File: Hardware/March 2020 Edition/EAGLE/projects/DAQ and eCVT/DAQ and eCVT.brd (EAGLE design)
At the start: 88.9 x 114 mm, 21 parts, among them J1 5558342-1, J2 5558342-1, J3 5558342-1, J4 5558342-1, U1 AP2114H-3.3TRG1

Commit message: Wiring the board...
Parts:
- removed D1: LTST-C170TBKT, LED:DIOC200X125X110
- added LED1: (no value), led:CHIPLED_0805
- moved R5 16.5 mm to (-3.81, 73.7)
- moved C1 7.41 mm to (31.8, 50.8)
- moved C2 7.41 mm to (31.8, 55.9)
- moved U1 7.41 mm to (25.4, 53.3)
- moved R1 2.54 mm to (8.89, 78.7)
- moved R3 2.54 mm to (8.89, 82.5)
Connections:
- removed net DAQ_ECVT\_MISO: U$31.12/MISO
- removed net N$34: D1.-, R5.1
- new net N$1: LED1.A, R5.2
- net +3V3: now also R5.1; no longer D1.+
- net DAQ_ECVT_MISO: now also U$31.12/MISO
- net GND: now also LED1.C; no longer R5.2
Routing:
- net DAQ_XBEE_MISO: track 0.00 -> 84.9 mm
- net DAQ_XBEE_RX: track 9.86 -> 68.3 mm, vias 0 -> 1
- net DAQ_XBEE_TX: track 9.09 -> 67.3 mm
- net DAQ_ECVT_TX: track 0.00 -> 19.9 mm, vias 0 -> 1
- net DAQ_ECVT_MOSI: track 0.00 -> 18.8 mm
- net DAQ_ECVT_MISO: track 0.00 -> 18.8 mm
- net DAQ_ECVT_SCK: track 0.00 -> 18.8 mm
- net DAQ_ECVT_CS: track 0.00 -> 13.2 mm
- net RBRAKE_PRESSURE: track 38.2 -> 35.7 mm
- net FBRAKE_PRESSURE: track 36.9 -> 34.4 mm
- net FRWHEEL_SPEED: track 84.2 -> 86.3 mm
- net SMOT_INB: track 54.1 -> 55.9 mm
- net SENC_A: track 59.1 -> 60.8 mm
- net DAQ_XBEE_MOSI: track 72.6 -> 73.9 mm
- net SMOT_INA: track 48.6 -> 49.8 mm
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
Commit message: Wiring the board...
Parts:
- moved C1 6.84 mm to (25.4, 48.3)
- moved C2 6.84 mm to (25.4, 58.4)
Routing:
- net DAQ_SPARE_A17_PWM: track 0.00 -> 52.8 mm, vias 0 -> 1
- net DAQ_SPARE_A18_PWM_SCL: track 0.00 -> 48.9 mm, vias 0 -> 1
- net DAQ_SPARE_A16_PWM: track 0.00 -> 48.0 mm, vias 0 -> 1
- net SMOT_CS: track 0.00 -> 47.4 mm, vias 0 -> 1
- net DAQ_SPARE_A21_DAC0: track 0.00 -> 47.2 mm, vias 0 -> 1
- net DAQ_SPARE_A19_PWM_SDA: track 0.00 -> 46.4 mm, vias 0 -> 1
- net DAQ_SPARE_A22_DAC1: track 0.00 -> 45.4 mm, vias 0 -> 1
- net PMOT_CS: track 0.00 -> 41.0 mm, vias 0 -> 3
- net ECVT_SPARE_A22_DAC1: track 0.00 -> 26.5 mm
- net ECVT_SPARE_A21_DAC0: track 0.00 -> 22.3 mm
- net DAQ_ECVT_CS: track 13.2 -> 18.8 mm, vias 0 -> 1
- net FLWHEEL_SPEED: track 81.2 -> 76.0 mm
- net FRWHEEL_SPEED: track 86.3 -> 81.1 mm
- net RBRAKE_PRESSURE: track 35.7 -> 38.2 mm
- net PMOT_INB: track 36.0 -> 37.8 mm
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
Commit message: Wiring the board...
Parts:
- moved C1 38.2 mm to (-12.7, 45.7)
- moved C2 38.2 mm to (-12.7, 55.9)
- moved U1 38.2 mm to (-12.7, 50.8)
- moved R5 9.25 mm to (-12.7, 76.2)
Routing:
- net DAQ_SPARE_A16_PWM: track 48.0 -> 120.1 mm
- net DAQ_SPARE_A17_PWM: track 52.8 -> 124.7 mm, vias 1 -> 3
- net DAQ_SPARE_A18_PWM_SCL: track 48.9 -> 118.2 mm
- net DAQ_SPARE_A19_PWM_SDA: track 46.4 -> 113.2 mm
- net DAQ_SPARE_A21_DAC0: track 47.2 -> 113.7 mm, vias 1 -> 3
- net DAQ_SPARE_A22_DAC1: track 45.4 -> 109.4 mm
- net ECVT_SPARE_A22_DAC1: track 26.5 -> 90.4 mm, vias 0 -> 4
- net ECVT_SPARE_A21_DAC0: track 22.3 -> 84.5 mm
- net PMOT_CS: track 41.0 -> 33.7 mm, vias 3 -> 2
- net FRWHEEL_SPEED: track 81.1 -> 83.1 mm
- net FLWHEEL_SPEED: track 76.0 -> 78.0 mm
- net RBRAKE_PRESSURE: track 38.2 -> 36.7 mm
- net FBRAKE_PRESSURE: track 34.4 -> 34.9 mm
- net RWHEELS_SPEED: vias 1 -> 2
- net ENGINE_SPEED: vias 2 -> 1

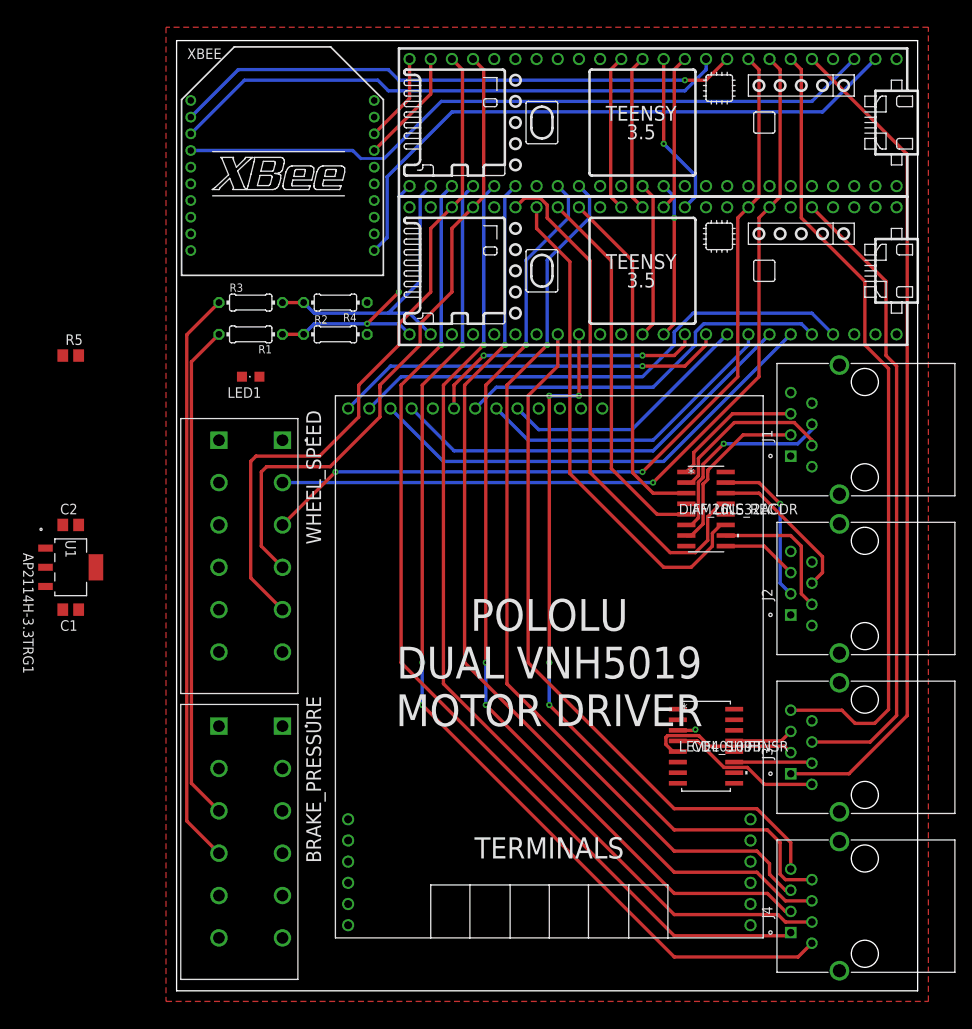
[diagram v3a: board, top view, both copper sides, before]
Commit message: Checkpoint before rewiring spring terminals to front/back instead of wheelspeed/brakepressure
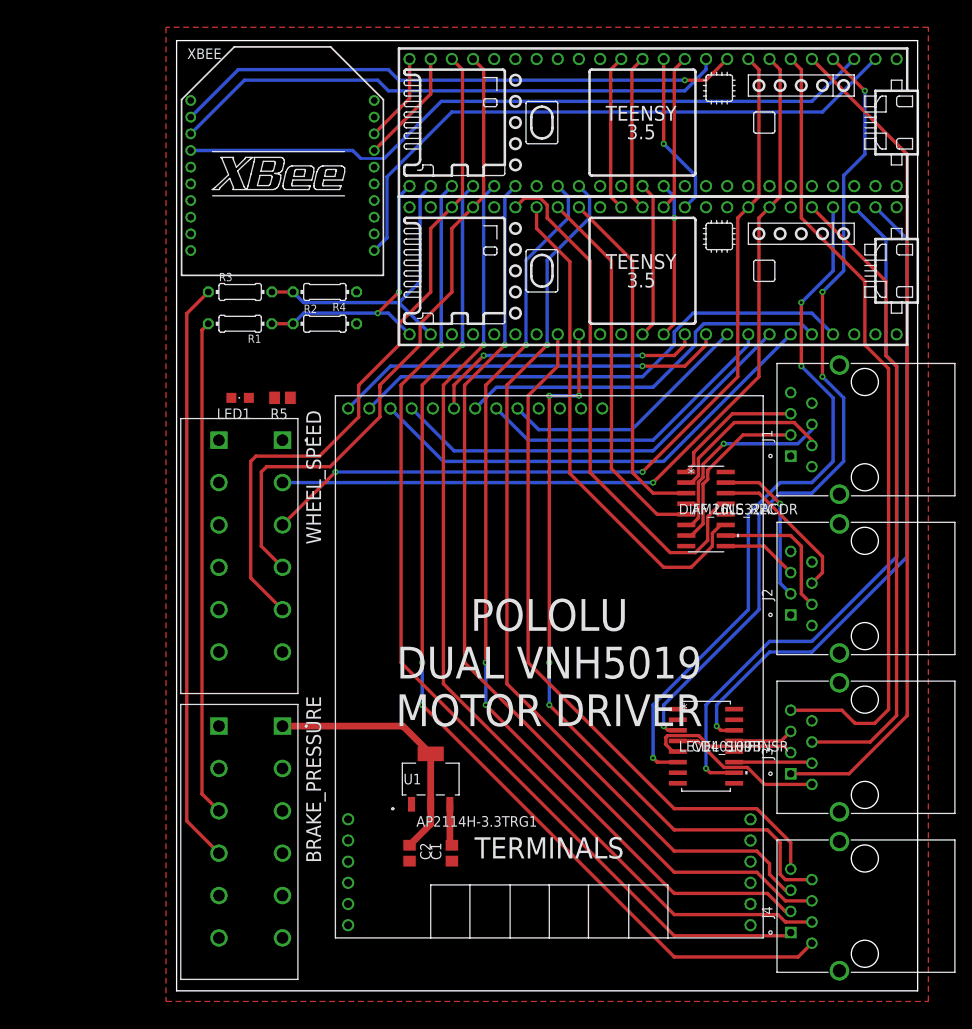
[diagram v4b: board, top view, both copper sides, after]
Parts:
- moved C2 56.6 mm to (27.9, 16.5), turned to 270 degrees
- moved C1 54.3 mm to (33.0, 16.5), turned to 270 degrees
- moved U1 50.1 mm to (30.5, 25.4), turned to 0 degrees
- moved R5 25.9 mm to (12.7, 71.1), turned to 180 degrees
- moved LED1 2.84 mm to (7.62, 71.1)
- moved R1 1.80 mm to (7.62, 80.0)
- moved R2 1.80 mm to (17.8, 80.0)
- moved R3 1.80 mm to (7.62, 83.8)
- moved R4 1.80 mm to (17.8, 83.8)
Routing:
- net DAQ_STATUS_LED: track 2.15 -> 97.8 mm, vias 1 -> 4
- net BKSHIFT_LED: track 0.00 -> 85.4 mm, vias 0 -> 1
- net ECVT_STATUS_LED: track 0.00 -> 83.6 mm, vias 0 -> 3
- net UPSHIFT_LED: track 0.00 -> 78.6 mm, vias 0 -> 1
- net +3V3: track 0.00 -> 31.2 mm
- net +5V: track 0.00 -> 5.01 mm
- net RBRAKE_PRESSURE_W/O_RES: track 69.2 -> 70.0 mm

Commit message: Almost done wiring the board!
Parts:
- moved R1 1.27 mm to (7.62, 81.3), turned to 0 degrees
- moved R2 1.27 mm to (17.8, 81.3)
- turned R4 to 0 degrees
- renumbered BRAKE_PRESSURE to FRONT_SENSORS, WHEEL_SPEED to REAR_SENSORS
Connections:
- net N$1 renamed LED
- removed net FBRAKE_PRESSURE_W/O_RES: FRONT_SENSORS.3_A, FRONT_SENSORS.3_B, R1.2
- removed net RBRAKE_PRESSURE_W/O_RES: FRONT_SENSORS.4_A, FRONT_SENSORS.4_B, R3.1
- new net FBRAKE_PRESSURE_BEFORE_RESISTORS: FRONT_SENSORS.5_A, FRONT_SENSORS.5_B, R3.1
- new net RBRAKE_PRESSURE_BEFORE_RESISTORS: R1.1, REAR_SENSORS.5_A, REAR_SENSORS.5_B
- net +3V3: now also REAR_SENSORS.1_A, REAR_SENSORS.1_B
- net +5V: now also REAR_SENSORS.2_A, REAR_SENSORS.2_B; no longer REAR_SENSORS.1_A, REAR_SENSORS.1_B
- net ENGINE_SPEED: now also REAR_SENSORS.3_A, REAR_SENSORS.3_B; no longer REAR_SENSORS.2_A, REAR_SENSORS.2_B
- net FBRAKE_PRESSURE: now also R3.2, R4.2; no longer R1.1, R2.1
- net FLWHEEL_SPEED: now also FRONT_SENSORS.3_A, FRONT_SENSORS.3_B; no longer REAR_SENSORS.4_A, REAR_SENSORS.4_B
- net FRWHEEL_SPEED: now also FRONT_SENSORS.4_A, FRONT_SENSORS.4_B; no longer REAR_SENSORS.5_A, REAR_SENSORS.5_B
- net GND: now also R2.1; no longer FRONT_SENSORS.5_A, FRONT_SENSORS.5_B, R2.2
- net RBRAKE_PRESSURE: now also R1.2, R2.2; no longer R3.2, R4.2
- net RWHEELS_SPEED: now also REAR_SENSORS.4_A, REAR_SENSORS.4_B; no longer REAR_SENSORS.3_A, REAR_SENSORS.3_B
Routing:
- net +5V: track 5.01 -> 164.5 mm, vias 0 -> 4
- net FBRAKE_PRESSURE_BEFORE_RESISTORS: track 0.00 -> 75.1 mm
- net RBRAKE_PRESSURE_W/O_RES: track 70.0 -> 0.00 mm
- net FBRAKE_PRESSURE_W/O_RES: track 59.6 -> 0.00 mm
- net +12V: track 0.00 -> 44.9 mm, vias 0 -> 2
- net RBRAKE_PRESSURE_BEFORE_RESISTORS: track 0.00 -> 37.1 mm
- net FRWHEEL_SPEED: track 83.1 -> 113.4 mm
- net FLWHEEL_SPEED: track 78.0 -> 108.3 mm
- net GND: track 0.00 -> 25.4 mm, vias 0 -> 5
- net RWHEELS_SPEED: track 101.7 -> 110.3 mm, vias 2 -> 1
- net RBRAKE_PRESSURE: track 36.7 -> 40.1 mm
- net +3V3: track 31.2 -> 34.5 mm, vias 0 -> 4
- net LED: track 0.00 -> 3.08 mm
- net FBRAKE_PRESSURE: track 34.9 -> 37.5 mm, vias 2 -> 1
- net ENGINE_SPEED: track 102.1 -> 104.2 mm
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- added copper zone on layer 16, net +3V3

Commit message: No DRC errors! Need to do a final check + board writing
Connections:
- removed net N$19: U$33.3V3
- removed net N$2: U$31.3V3
- net +3V3: now also U$31.3V3, U$33.3V3
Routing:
- net +5V: track 164.5 -> 179.7 mm
- net RWHEELS_SPEED: track 110.3 -> 118.7 mm, vias 1 -> 2
- net FRWHEEL_SPEED: track 113.4 -> 121.0 mm
- net FLWHEEL_SPEED: track 108.3 -> 115.9 mm
- net FBRAKE_PRESSURE_BEFORE_RESISTORS: track 75.1 -> 82.7 mm
- net ENGINE_SPEED: track 104.2 -> 111.8 mm
- net RBRAKE_PRESSURE_BEFORE_RESISTORS: track 37.1 -> 44.8 mm
- net +3V3: track 34.5 -> 38.3 mm, vias 4 -> 6
- net DAQ_STATUS_LED_12V: track 18.8 -> 18.2 mm

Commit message: Small board revisions before sending out
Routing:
- net +5V: track 179.7 -> 207.9 mm, vias 4 -> 5
- net DAQ_SPARE_A17_PWM: track 125.6 -> 126.5 mm, vias 4 -> 3
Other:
- board text added: "+3.3V OUT +5V IN/OUT ENGINE IN RWHEELS IN RBRAKES IN GROUND"
- board text added: "+3.3V OUT +5V IN/OUT FLWHEEL IN FRWHEEL IN FBRAKES IN GROUND"
- board text added: "DASHBOARD"
- board text added: "DESIGNED BY RAHUL GOYAL MARCH 2020"
- board text added: "PRIMARY ENCODER"
- board text added: "SECONDARY ENCODER"
- board text added: "SPARES"
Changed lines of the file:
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@@
 <drawing>
 <settings>
-<setting alwaysvectorfont="no"/>
+<setting alwaysvectorfont="yes"/>
 <setting verticaltext="up"/>
 </settings>
@@
 <wire x1="88.88" y1="113.97" x2="0" y2="113.97" width="0" layer="20"/>
 <wire x1="0" y1="113.97" x2="0" y2="0" width="0" layer="20"/>
-<hole x="19.05" y="76.2" drill="4.3053"/>
-<hole x="19.05" y="3.175" drill="4.3053"/>
-<hole x="69.85" y="3.175" drill="4.3053"/>
+<hole x="19.05" y="76.2" drill="3.6576"/>
+<hole x="22.225" y="3.175" drill="3.6576"/>
+<hole x="66.675" y="3.175" drill="3.6576"/>
+<text x="9.525" y="76.2" size="1.27" layer="25" font="vector" ratio="25" align="center">DESIGNED BY
+RAHUL GOYAL
+MARCH 2020</text>
+<text x="44.45" y="86.36" size="2.54" layer="26" font="vector" ratio="25" rot="MR0" align="center">DESIGNED BY
+RAHUL GOYAL
+MARCH 2020</text>
+<text x="25.4" y="40.005" size="1.6764" layer="26" font="vector" ratio="25" rot="MR0" align="bottom-right">+3.3V OUT
++5V IN/OUT
+ENGINE IN
+RWHEELS IN
+RBRAKES IN
+GROUND</text>
+<text x="25.4" y="5.715" size="1.6764" layer="26" font="vector" ratio="25" rot="MR0" align="bottom-right">+3.3V OUT
++5V IN/OUT
+FLWHEEL IN
+FRWHEEL IN
+FBRAKES IN
+GROUND</text>
+<text x="63.5" y="10.16" size="1.6764" layer="26" font="vector" ratio="25" rot="MR0" align="center-left">SPARES</text>
+<text x="63.5" y="29.21" size="1.6764" layer="26" font="vector" ratio="25" rot="MR0" align="center-left">DASHBOARD</text>
+<text x="63.5" y="48.26" size="1.6764" layer="26" font="vector" ratio="25" rot="MR0" align="center-left">SECONDARY
+ENCODER</text>
+<text x="63.5" y="67.31" size="1.6764" layer="26" font="vector" ratio="25" rot="MR0" align="center-left">PRIMARY
+ENCODER</text>
 </plain>
 <attributes>
@@
 <contactref element="REAR_SENSORS" pad="3_A"/>
 <contactref element="REAR_SENSORS" pad="3_B"/>
-<wire x1="58.42" y1="62.23" x2="52.07" y2="55.88" width="0.4064" layer="16"/>
-<wire x1="52.07" y1="55.88" x2="12.7" y2="55.88" width="0.4064" layer="16"/>
 <wire x1="5.08" y1="55.88" x2="12.7" y2="55.88" width="0.4064" layer="16"/>
+<wire x1="12.7" y1="55.88" x2="13.97" y2="57.15" width="0.4064" layer="16"/>
+<wire x1="53.34" y1="57.15" x2="58.42" y2="62.23" width="0.4064" layer="16"/>
+<wire x1="13.97" y1="57.15" x2="53.34" y2="57.15" width="0.4064" layer="16"/>
 </signal>
 <signal name="RWHEELS_SPEED">
@@
 <contactref element="REAR_SENSORS" pad="4_B"/>
 <contactref element="REAR_SENSORS" pad="4_A"/>
-<wire x1="52.07" y1="58.42" x2="55.88" y2="62.23" width="0.4064" layer="16"/>
 <wire x1="5.08" y1="50.8" x2="12.7" y2="50.8" width="0.4064" layer="16"/>
 <via x="10.16" y="57.15" extent="1-16" drill="0.35"/>
-<wire x1="10.16" y1="57.15" x2="11.43" y2="58.42" width="0.4064" layer="16"/>
-<wire x1="11.43" y1="58.42" x2="52.07" y2="58.42" width="0.4064" layer="16"/>
 <wire x1="10.16" y1="53.34" x2="12.7" y2="50.8" width="0.4064" layer="1"/>
 <wire x1="10.16" y1="57.15" x2="10.16" y2="53.34" width="0.4064" layer="1"/>
+<wire x1="10.16" y1="57.15" x2="12.065" y2="59.055" width="0.4064" layer="16"/>
+<wire x1="52.705" y1="59.055" x2="55.88" y2="62.23" width="0.4064" layer="16"/>
+<wire x1="12.065" y1="59.055" x2="52.705" y2="59.055" width="0.4064" layer="16"/>
 </signal>
 <signal name="DAQ_XBEE_RX">
@@
 <via x="29.464" y="34.29" extent="1-16" drill="0.35"/>
 <wire x1="29.464" y1="72.644" x2="29.464" y2="39.37" width="0.4064" layer="1"/>
-<wire x1="29.464" y1="34.29" x2="59.817" y2="3.937" width="0.4064" layer="1"/>
-<wire x1="76.2" y1="5.715" x2="72.07851875" y2="5.715" width="0.4064" layer="16"/>
-<wire x1="72.07851875" y1="5.715" x2="71.24666875" y2="6.54685" width="0.4064" layer="16"/>
-<via x="64.77" y="3.81" extent="1-16" drill="0.35"/>
-<wire x1="64.77" y1="3.81" x2="59.944" y2="3.81" width="0.4064" layer="1"/>
-<wire x1="59.944" y1="3.81" x2="59.817" y2="3.937" width="0.4064" layer="1"/>
-<wire x1="71.24666875" y1="6.54685" x2="67.50685" y2="6.54685" width="0.4064" layer="16"/>
-<wire x1="67.50685" y1="6.54685" x2="64.77" y2="3.81" width="0.4064" layer="16"/>
+<wire x1="59.944" y1="3.81" x2="29.464" y2="34.29" width="0.4064" layer="1"/>
+<wire x1="74.295" y1="3.81" x2="76.2" y2="5.715" width="0.4064" layer="1"/>
+<wire x1="64.77" y1="5.715" x2="68.58" y2="5.715" width="0.4064" layer="1"/>
+<wire x1="62.865" y1="3.81" x2="59.944" y2="3.81" width="0.4064" layer="1"/>
+<wire x1="64.77" y1="5.715" x2="62.865" y2="3.81" width="0.4064" layer="1"/>
+<wire x1="71.12" y1="3.81" x2="74.295" y2="3.81" width="0.4064" layer="1"/>
+<wire x1="70.485" y1="3.81" x2="71.12" y2="3.81" width="0.4064" layer="1"/>
+<wire x1="68.58" y1="5.715" x2="70.485" y2="3.81" width="0.4064" layer="1"/>
 </signal>
 <signal name="DAQ_SPARE_A18_PWM_SCL">
@@
 <wire x1="45.72" y1="93.98" x2="52.07" y2="87.63" width="0.4064" layer="1"/>
 <wire x1="52.07" y1="87.63" x2="52.07" y2="71.64860625" width="0.4064" layer="1"/>
-<wire x1="57.62973125" y1="57.15" x2="53.34" y2="61.43973125" width="0.4064" layer="1"/>
+<wire x1="57.62973125" y1="57.15" x2="56.119865625" y2="58.659865625" width="0.4064" layer="1"/>
+<wire x1="56.119865625" y1="58.659865625" x2="53.34" y2="61.43973125" width="0.4064" layer="1"/>
 <wire x1="53.34" y1="70.37860625" x2="52.07" y2="71.64860625" width="0.4064" layer="1"/>
 <wire x1="53.34" y1="61.43973125" x2="53.34" y2="70.37860625" width="0.4064" layer="1"/>
@@
 <contactref element="REAR_SENSORS" pad="2_B"/>
 <contactref element="REAR_SENSORS" pad="2_A"/>
-<via x="31.75" y="25.4" extent="1-16" drill="0.35"/>
-<wire x1="31.75" y1="25.4" x2="32.78" y2="24.37" width="0.8128" layer="1"/>
-<wire x1="32.78" y1="24.37" x2="32.78" y2="22.375" width="0.8128" layer="1"/>
+<wire x1="29.21" y1="26.67" x2="32.78" y2="23.1" width="0.8128" layer="1"/>
+<wire x1="32.78" y1="23.1" x2="32.78" y2="22.375" width="0.8128" layer="1"/>
 <wire x1="65.8622" y1="62.23" x2="70.485" y2="62.23" width="0.8128" layer="1"/>
 <wire x1="70.485" y1="62.23" x2="74.93" y2="57.785" width="0.8128" layer="1"/>
@@
 <wire x1="74.93" y1="57.785" x2="74.93" y2="53.975" width="0.8128" layer="16"/>
 <wire x1="74.93" y1="53.975" x2="73.66" y2="52.705" width="0.8128" layer="16"/>
-<wire x1="31.75" y1="25.4" x2="40.9575" y2="34.6075" width="0.8128" layer="16"/>
 <wire x1="73.66" y1="71.755" x2="69.85" y2="71.755" width="0.8128" layer="16"/>
-<wire x1="40.9575" y1="42.8625" x2="40.9575" y2="34.6075" width="0.8128" layer="16"/>
 <wire x1="69.85" y1="71.755" x2="61.595" y2="63.5" width="0.8128" layer="16"/>
 <wire x1="61.595" y1="63.5" x2="56.515" y2="58.42" width="0.8128" layer="16"/>
-<wire x1="56.515" y1="58.42" x2="40.9575" y2="42.8625" width="0.8128" layer="16"/>
 <wire x1="61.1378" y1="58.42" x2="58.42" y2="58.42" width="0.8128" layer="1"/>
 <via x="58.42" y="58.42" extent="1-16" drill="0.35"/>
@@
 <wire x1="69.85" y1="63.5" x2="61.595" y2="63.5" width="0.8128" layer="16"/>
 <wire x1="12.7" y1="60.96" x2="19.05" y2="54.61" width="0.8128" layer="1"/>
-<wire x1="19.05" y1="33.02" x2="25.4" y2="26.67" width="0.8128" layer="1"/>
-<wire x1="19.05" y1="54.61" x2="19.05" y2="33.02" width="0.8128" layer="1"/>
-<wire x1="12.7" y1="26.67" x2="25.4" y2="26.67" width="0.8128" layer="1"/>
-<wire x1="25.4" y1="26.67" x2="26.67" y2="25.4" width="0.8128" layer="1"/>
-<wire x1="26.67" y1="25.4" x2="31.75" y2="25.4" width="0.8128" layer="1"/>
 <wire x1="5.08" y1="26.67" x2="12.7" y2="26.67" width="0.4064" layer="16"/>
 <wire x1="5.08" y1="60.96" x2="12.7" y2="60.96" width="0.4064" layer="16"/>
+<via x="19.05" y="54.61" extent="1-16" drill="0.35"/>
+<wire x1="12.7" y1="26.67" x2="25.4" y2="26.67" width="0.8128" layer="1"/>
+<wire x1="19.05" y1="54.61" x2="19.05" y2="33.02" width="0.8128" layer="1"/>
+<wire x1="19.05" y1="33.02" x2="12.7" y2="26.67" width="0.8128" layer="1"/>
+<via x="19.05" y="33.02" extent="1-16" drill="0.35"/>
+<wire x1="19.05" y1="33.02" x2="25.4" y2="26.67" width="0.8128" layer="1"/>
+<wire x1="25.4" y1="26.67" x2="29.21" y2="26.67" width="0.8128" layer="1"/>
+<wire x1="19.05" y1="33.02" x2="29.845" y2="43.815" width="0.8128" layer="16"/>
+<wire x1="19.05" y1="54.61" x2="29.845" y2="43.815" width="0.8128" layer="16"/>
+<wire x1="41.91" y1="43.815" x2="56.515" y2="58.42" width="0.8128" layer="16"/>
+<wire x1="29.845" y1="43.815" x2="41.91" y2="43.815" width="0.8128" layer="16"/>
 </signal>
 <signal name="N$43">
@@
 <wire x1="48.514" y1="69.85" x2="48.514" y2="62.23" width="0.4064" layer="1"/>
 <via x="48.514" y="62.23" extent="1-16" drill="0.35"/>
-<wire x1="48.514" y1="62.23" x2="48.514" y2="61.214" width="0.8128" layer="16"/>
-<wire x1="48.514" y1="61.214" x2="46.99" y2="59.69" width="0.8128" layer="16"/>
-<via x="46.99" y="59.69" extent="1-16" drill="0.35"/>
+<wire x1="48.514" y1="62.23" x2="46.99" y2="60.706" width="0.8128" layer="16"/>
+<via x="46.99" y="60.706" extent="1-16" drill="0.35"/>
 <wire x1="46.99" y1="53.6702" x2="66.8782" y2="33.782" width="0.8128" layer="1"/>
-<wire x1="46.99" y1="59.69" x2="46.99" y2="53.6702" width="0.8128" layer="1"/>
+<wire x1="46.99" y1="60.706" x2="46.99" y2="53.6702" width="0.8128" layer="1"/>
 </signal>
 <signal name="UPSHIFT_LED_12V">

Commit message: Ready to send out
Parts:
- moved U$31 1.27 mm to (87.6, 114.3)
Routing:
- net GND: track 25.4 -> 29.0 mm, vias 5 -> 6
- net RWHEELS_SPEED: track 118.7 -> 120.0 mm
- net DAQ_SPARE_A22_DAC1: track 109.4 -> 110.6 mm
- net DAQ_SPARE_A21_DAC0: track 113.7 -> 115.0 mm
- net DAQ_SPARE_A19_PWM_SDA: track 113.2 -> 114.4 mm
- net DAQ_SPARE_A18_PWM_SCL: track 118.2 -> 119.5 mm
- net DAQ_SPARE_A17_PWM: track 126.5 -> 127.8 mm
- net DAQ_SPARE_A16_PWM: track 120.1 -> 121.4 mm
- net DAQ_ECVT_CS: track 18.8 -> 20.1 mm
- net RBRAKE_PRESSURE: track 40.1 -> 41.3 mm
- net DAQ_ECVT_SCK: track 18.8 -> 20.1 mm
- net DAQ_ECVT_RX: track 18.8 -> 20.1 mm
- net DAQ_ECVT_MOSI: track 18.8 -> 20.1 mm
- net DAQ_ECVT_MISO: track 18.8 -> 20.1 mm
- net MARKER_BUTTON: track 95.9 -> 97.2 mm
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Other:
- board size 88.9 x 114 mm -> 88.9 x 114.3 mm
